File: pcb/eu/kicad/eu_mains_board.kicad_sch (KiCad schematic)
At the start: 10 parts, among them J1 2604-3102, J2 2604-3102, J3 TSM-102-01-L-SV

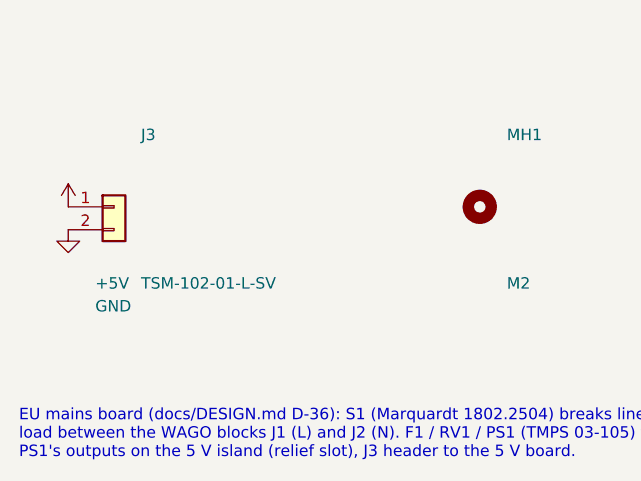
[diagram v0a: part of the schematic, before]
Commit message: Boards for v0.4: ring board, mic carrier, riser, cover flex, EU cap board, wiring board posts
- Ring board, mic carrier and riser in pcb/sensor/ (D-50, D-60, D-68); carrier and riser fab
  packs; the ring board waits on the MSR-2's CN2 part and map
- Riser 14 x 12 mm, pins above and between the posts; cover flex with the run past the GND
  contact post and a jog from the pad section (D-79)
- EU cap board on the carrier, closed snap windows, wider with the face plate (D-56, D-70,
  D-77, D-78); EU 5 V board pins follow the back cover's pads
- Wiring board: WA-SMSI spacer posts in the 5 V area (SMT, spigot inside the board), J2
- ERC / DRC clean on every board
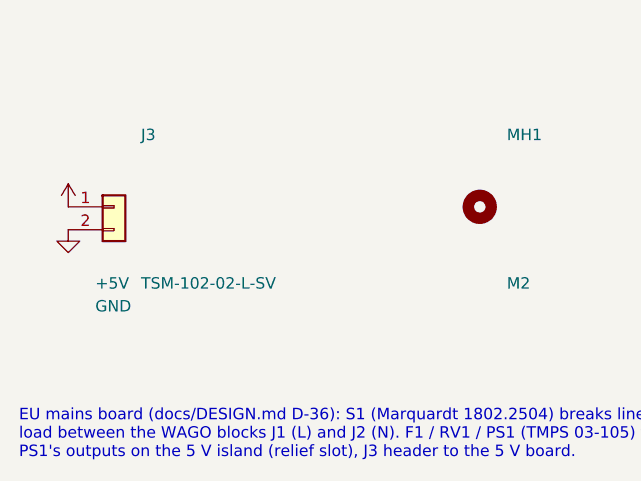
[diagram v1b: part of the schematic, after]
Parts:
- J3: value TSM-102-01-L-SV -> TSM-102-02-L-SV; MPN TSM-102-01-L-SV -> TSM-102-02-L-SV
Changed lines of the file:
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@@
 	(title_block
 		(title "Smart wall plate - EU mains board")
-		(date "2026-10-09")
+		(date "2026-10-11")
 		(rev "v0.2")
 		(company "smart-wallplate")
@@
 			)
 		)
-		(property "Value" "TSM-102-01-L-SV"
+		(property "Value" "TSM-102-02-L-SV"
 			(at 38.56 165.98 0)
 			(effects
@@
 			)
 		)
-		(property "Description" "SMT pin header 1x2, 2.54 mm, 5.84 mm post, gold on post: 5 V to the 5 V board's pin socket (5 V island)"
+		(property "Description" "SMT pin header 1x2, 2.54 mm, 8.13 mm post, gold on post: 5 V to the 5 V board's pin socket (5 V island)"
 			(at 35.56 157.48 0)
 			(effects
@@
 			)
 		)
-		(property "MPN" "TSM-102-01-L-SV"
+		(property "MPN" "TSM-102-02-L-SV"
 			(at 35.56 157.48 0)
 			(effects

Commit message: Mic on the boards, parts audit, rocker second source, CN2 land pattern, back cover fit (D-82..D-90)
- Prototype PCBWay packs for the ring board, EU cap board and cover flex; logos and URL on the
  boards with room for them
- CN2 mate: Molex 55909-2474 on an assumed 51338-2474 (D-82); land pattern from Molex
  SD-55909-003 rev J, B2B from SD-51338-003 rev K (D-89); contact map and pin 1 still open
- Microphone: Knowles SPK0641HT4H-1 + ADAU7002 on the ring board and the EU cap board, the mic
  carrier removed; face plate sound column on a gasket (D-83); C3 KEMET C1206C104J3GACTU C0G
  (D-85)
- Parts rule (active, stocked at DigiKey or Mouser) and audit: F1 3403.0166.11, cover flex 1 uF
  CL05A105KO5NNNC, rocker at Mouser 979-1802.2504 (D-84)
- Rocker: tabs soldered into plated slots accepted (D-86); E-Switch RA412C1100 second source,
  slotted footprint on the wiring board and the EU mains board, solder the rocker after the
  board is screwed down (D-88)
- Back cover: round-over 8.1 x 8.0 from the printed gauges (D-87); four tabs inside the long
  side walls into the housing's slots (D-90); back_gauges_PLA
- make stock / make order-push (pcb/tools/distributors.py): live DigiKey / Mouser stock and
  lifecycle, DigiKey myLists link and Mouser cart; keys from the environment only
- Boards ERC / DRC clean; make check, make eu, make check-renders pass; renders, fab and
  order packs regenerated
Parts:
- F1: MPN 3404.2416.22 -> 3403.0166.11
- S1: footprint eu:Marquardt_1802.2504_DPST_PCB -> eu:Rocker_DPST_Marquardt_1802.2504_E-Switch_RA412C1100
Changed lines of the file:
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@@
 			)
 		)
-		(property "Footprint" "eu:Marquardt_1802.2504_DPST_PCB"
+		(property "Footprint" "eu:Rocker_DPST_Marquardt_1802.2504_E-Switch_RA412C1100"
 			(at 35.56 91.44 0)
 			(effects
@@
 			)
 		)
-		(property "MPN" "3404.2416.22"
-			(at 157.48 91.44 0)
-			(effects
+		(property "MPN" "3403.0166.11"
+			(at 157.48 91.44 0)
+			(effects

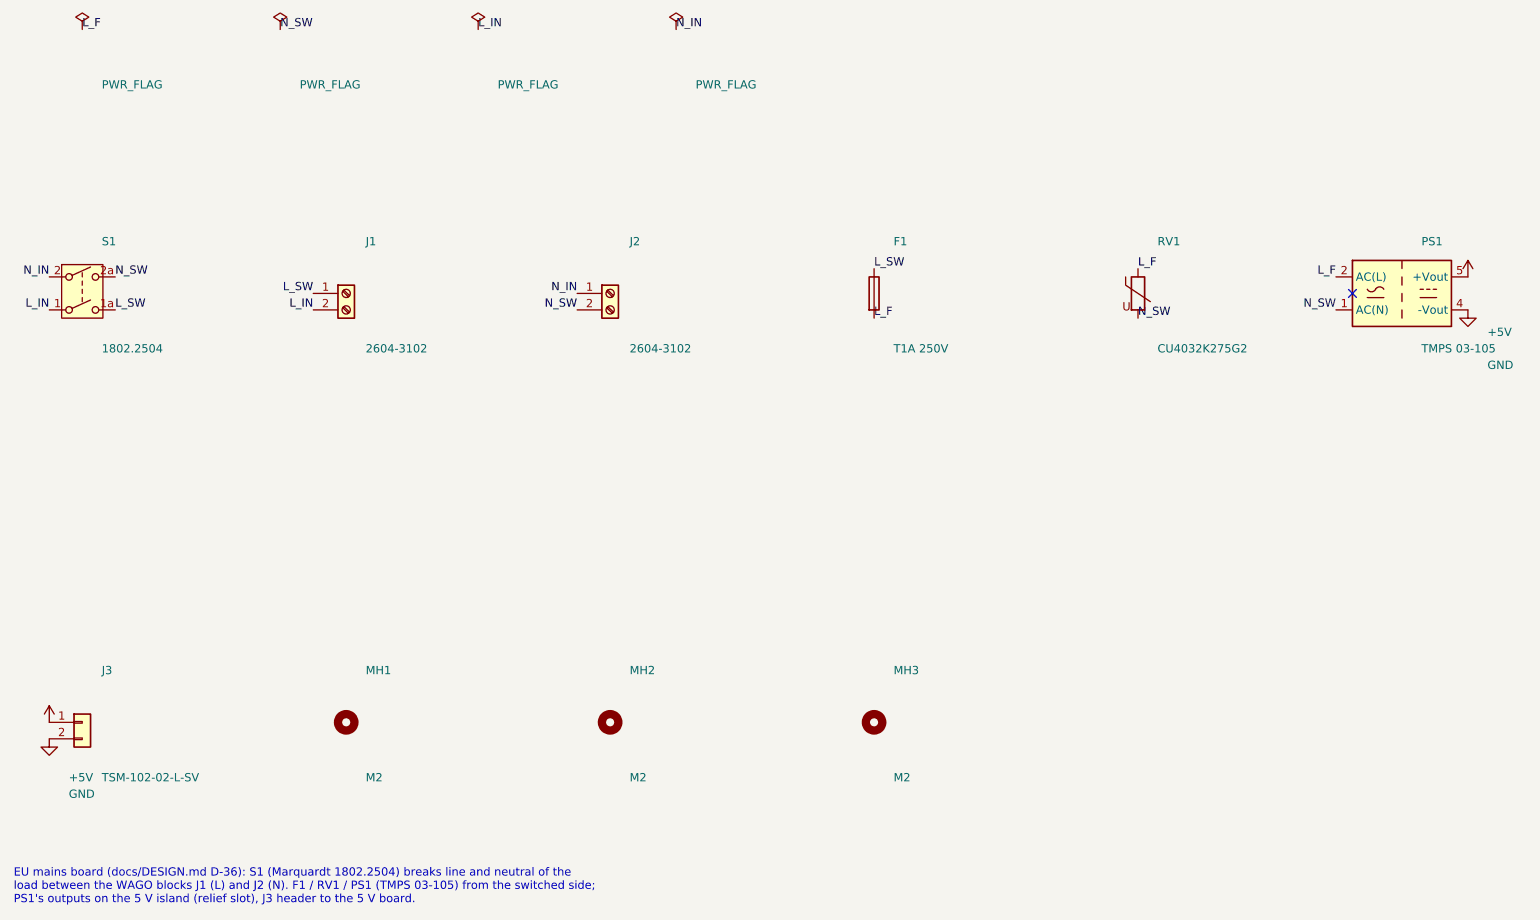
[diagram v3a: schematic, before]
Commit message: EU PSU: Zettler ZPI03S0500WC instead of the Traco TMPS 03-105 (D-100)
- 8.72 against 24.09 CAD at DigiKey (an EU plate's parts 63.54, was 78.91); 5 V 600 mA,
  I/P-O/P 3600 VAC, UL/EN 62368-1; body 25 x 25 x 16 +-0.5 (PSU the maximum)
- Footprint from Zettler's PCB layout (AC pins 15 apart, outputs 5 apart, rows 15 apart, 1.2
  holes), 4-pin symbol; the NC pin and its DRC rule removed
- Mains board re-laid: fused line track 3.5 from the N pin, relief slot y -15, 5 V header x 8.5
  beside V+, F1 (15.0, -2.5), front logos above the slot; both EU boards ERC / DRC clean,
  make eu passes
- Open for review: reinforced insulation and overvoltage category not stated; Zettler's input
  fuse 0.5 A (F1 is T1A); DigiKey stock 142
- Order lists, PCBWay packs and renders regenerated
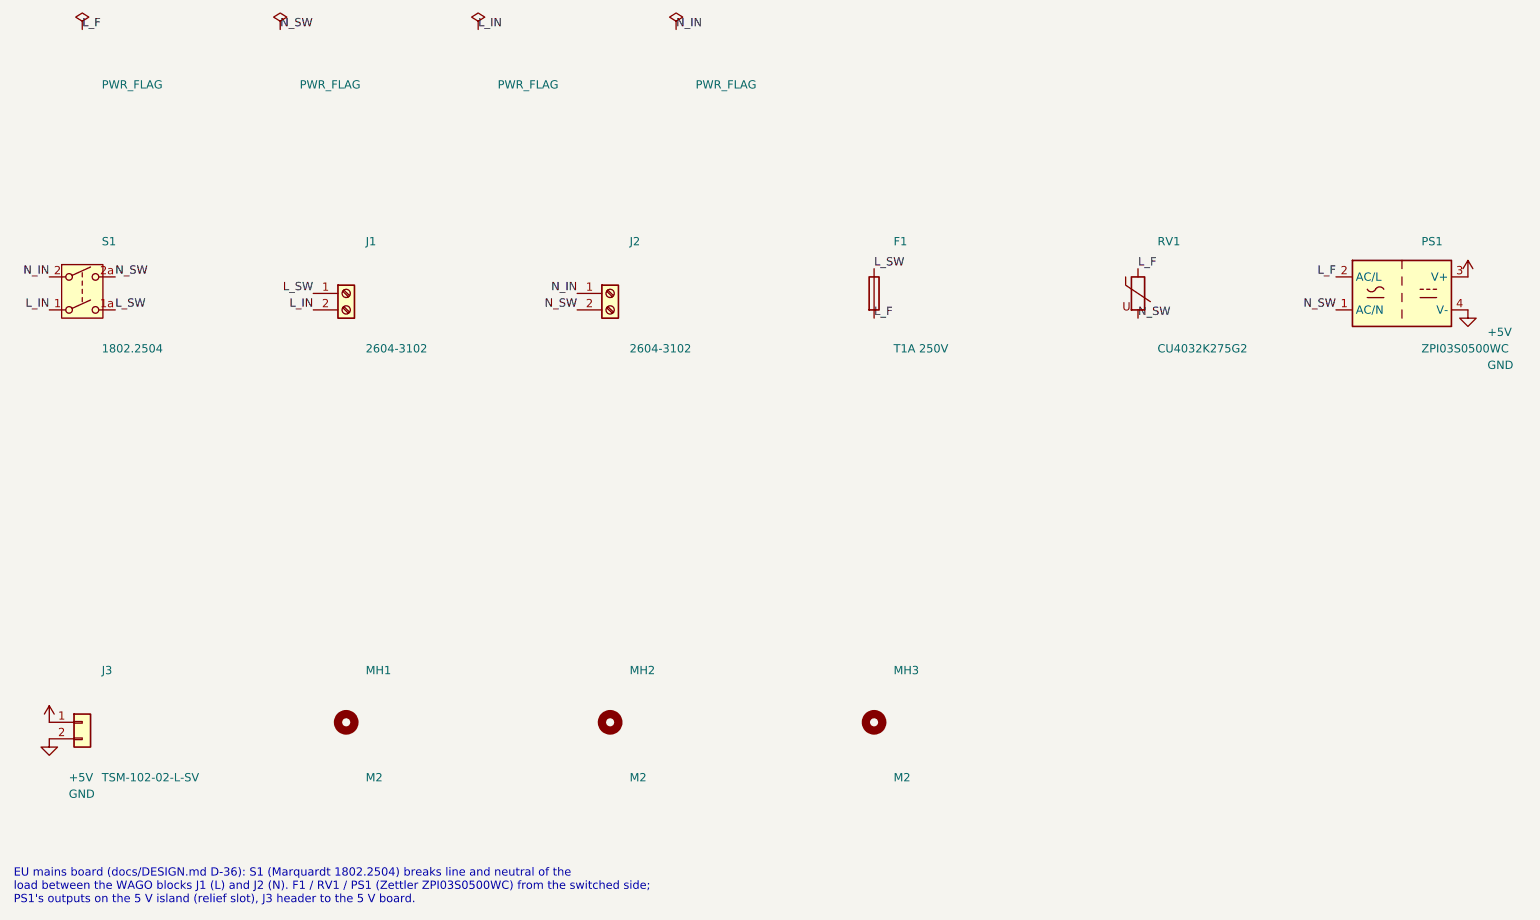
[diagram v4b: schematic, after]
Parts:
- PS1: value TMPS 03-105 -> ZPI03S0500WC; footprint eu:Converter_ACDC_TRACO_TMPS03_THT -> eu:Converter_ACDC_Zettler_ZPI03_THT; symbol eu:TMPS03-105 -> eu:ZPI03S0500WC; MPN TMPS 03-105 -> ZPI03S0500WC; Manufacturer Traco Power -> Zettler Magnetics
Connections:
- net +5V: now also PS1.3 (V+); no longer PS1.5 (+Vout)
- no-connect marks 1 -> 0
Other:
- note added: "EU mains board (docs/DESIGN.md D-36): S1 (Marquardt 1802.2504) breaks line and neutral of the load between the WAGO blocks J1 (L) and J2 (N). F1 / RV1 / PS1 (Zettler ZPI03S0500WC) from the switched side; PS1's outputs on the 5 V island (relief slot), J3 header to the 5 V board."
- note removed: "EU mains board (docs/DESIGN.md D-36): S1 (Marquardt 1802.2504) breaks line and neutral of the load between the WAGO blocks J1 (L) and J2 (N). F1 / RV1 / PS1 (TMPS 03-105) from the switched side; PS1's outputs on the 5 V island (relief slot), J3 header to the 5 V board."
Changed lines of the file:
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@@
 			)
 		)
-		(property "Description" "SMD fuse UMT 250, time-lag 1 A 250 VAC (TMPS 03 recommended input fuse T1.0 A / 250 V)"
+		(property "Description" "SMD fuse UMT 250, time-lag 1 A 250 VAC (Zettler's application circuit shows 0.5 A / 250 V: review, D-100)"
 			(at 157.48 91.44 0)
 			(effects
@@
 	)
 	(symbol
-		(lib_id "eu:TMPS03-105")
+		(lib_id "eu:ZPI03S0500WC")
 		(at 238.76 91.44 0)
 		(unit 1)
@@
 			)
 		)
-		(property "Value" "TMPS 03-105"
+		(property "Value" "ZPI03S0500WC"
 			(at 241.76 99.94 0)
 			(effects
@@
 			)
 		)
-		(property "Footprint" "eu:Converter_ACDC_TRACO_TMPS03_THT"
+		(property "Footprint" "eu:Converter_ACDC_Zettler_ZPI03_THT"
 			(at 238.76 91.44 0)
 			(effects
@@
 			)
 		)
-		(property "Datasheet" "https://www.tracopower.com/sites/default/files/products/datasheets/tmps03_datasheet.pdf"
+		(property "Datasheet" "https://www.zettlermagnetics.com/media/pdfs/magnetics/datasheets/ZPI03SXX00WC.pdf"
 			(at 238.76 91.44 0)
 			(effects
@@
 			)
 		)
-		(property "Description" "AC-DC module 85-264 VAC in, 5 V 600 mA, 25.4x25.4x16.3 mm, IEC/UL 62368-1, IEC 60335-1"
+		(property "Description" "AC-DC module 90-264 VAC in, 5 V 600 mA, 25x25x16 mm, I/P-O/P 3600 VAC, UL/EN 62368-1 (D-100)"
 			(at 238.76 91.44 0)
 			(effects
@@
 			)
 		)
-		(property "Manufacturer" "Traco Power"
+		(property "Manufacturer" "Zettler Magnetics"
 			(at 238.76 91.44 0)
 			(effects
@@
 			)
 		)
-		(property "MPN" "TMPS 03-105"
+		(property "MPN" "ZPI03S0500WC"
 			(at 238.76 91.44 0)
 			(effects
@@
 		)
 		(pin "3"
-		)
-		(pin "5"
 		)
 		(pin "4"
@@
 		)
 	)
-	(no_connect
-		(at 231.14 91.44)
-	)
 	(symbol
 		(lib_id "eu:+5V")
@@
 		)
 	)
-	(text "EU mains board (docs/DESIGN.md D-36): S1 (Marquardt 1802.2504) breaks line and neutral of the\nload between the WAGO blocks J1 (L) and J2 (N). F1 / RV1 / PS1 (TMPS 03-105) from the switched side;\nPS1's outputs on the 5 V island (relief slot), J3 header to the 5 V board."
+	(text "EU mains board (docs/DESIGN.md D-36): S1 (Marquardt 1802.2504) breaks line and neutral of the\nload between the WAGO blocks J1 (L) and J2 (N). F1 / RV1 / PS1 (Zettler ZPI03S0500WC) from the switched side;\nPS1's outputs on the 5 V island (relief slot), J3 header to the 5 V board."
 		(exclude_from_sim no)
 		(at 25 180 0)

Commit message: Flex review fixes, back cover clip, README, Sladdseg, order lists (D-116..D-119)
- D-116: cover flex: 0603 X5R input/output caps, ESD diode TPD1E10B06DYAR,
  0.6 mm bend radius with relief slits, stiffener notch and outlines,
  coverlay expansion, mask-defined pin pads, teardrops, fab notes; the
  cover's snap hooks allow for stiffener adhesive and tolerance
- D-117, D-118: bottom clip catch 3.22 above the floor, tip as far proud of
  the shell as the top clip's
- Battery polarity confirmed on a unit
- README rewritten: three editions, assembly renders, safety and polarity
  warnings, cost for 1 to 10,000 plates, printed parts; detail and board
  renders moved to their docs; the product is named Sladdseg
- EU boards: the ant logo on the other face
- D-119: order lists: one NA plate, one EU plate, a devkit of 5 + 5
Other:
- title: Smart wall plate - EU mains board -> Sladdseg - EU mains board
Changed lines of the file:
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@@
 	(paper "A4")
 	(title_block
-		(title "Smart wall plate - EU mains board")
+		(title "Sladdseg - EU mains board")
 		(date "2026-10-12")
 		(rev "v0.5")
